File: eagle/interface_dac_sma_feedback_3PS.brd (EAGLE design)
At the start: 95.6 x 144.9 mm, 36 parts, among them IC1 ISO1540, IC2 LT1352PA, IC3 LT1352PA, Q1 TIP122V, Q2 TIP122V, Q3 TIP122V, X1 BU-SMA-V

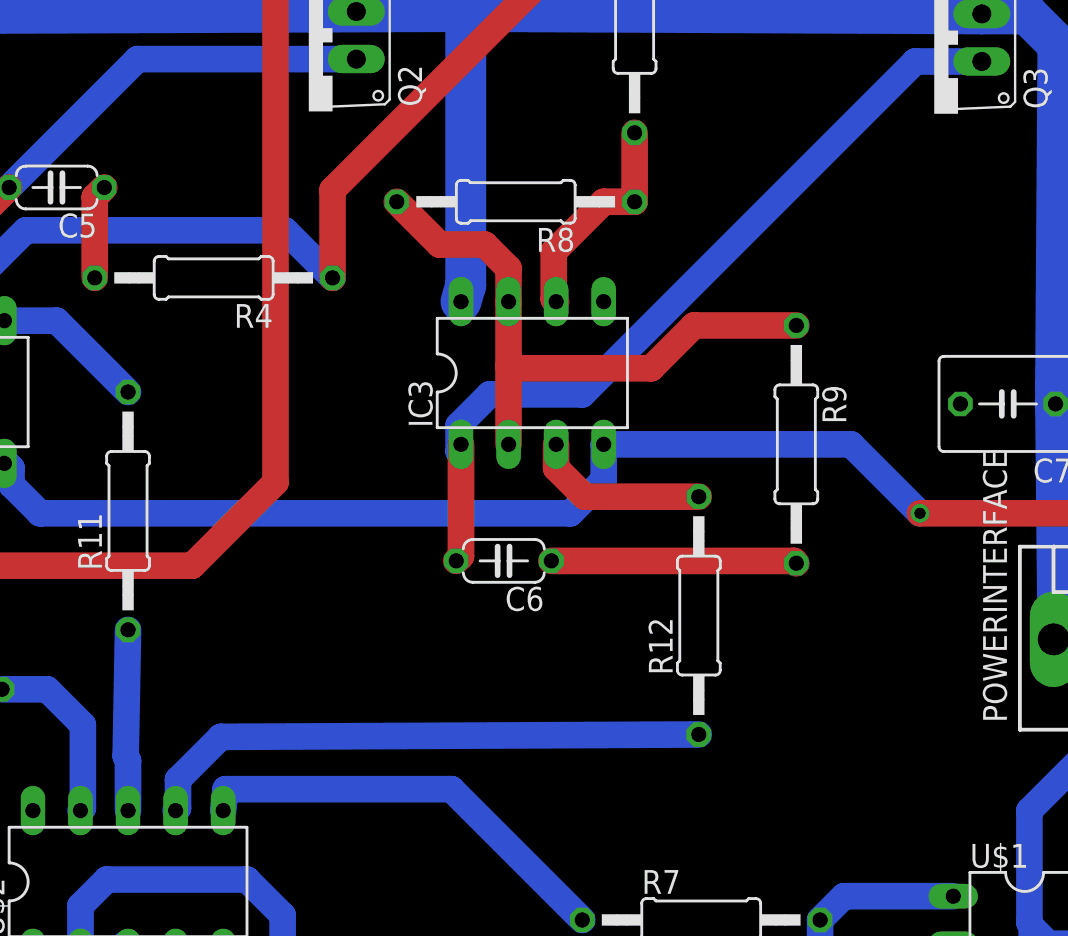
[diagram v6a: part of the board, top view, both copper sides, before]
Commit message: Fix negative rail problems
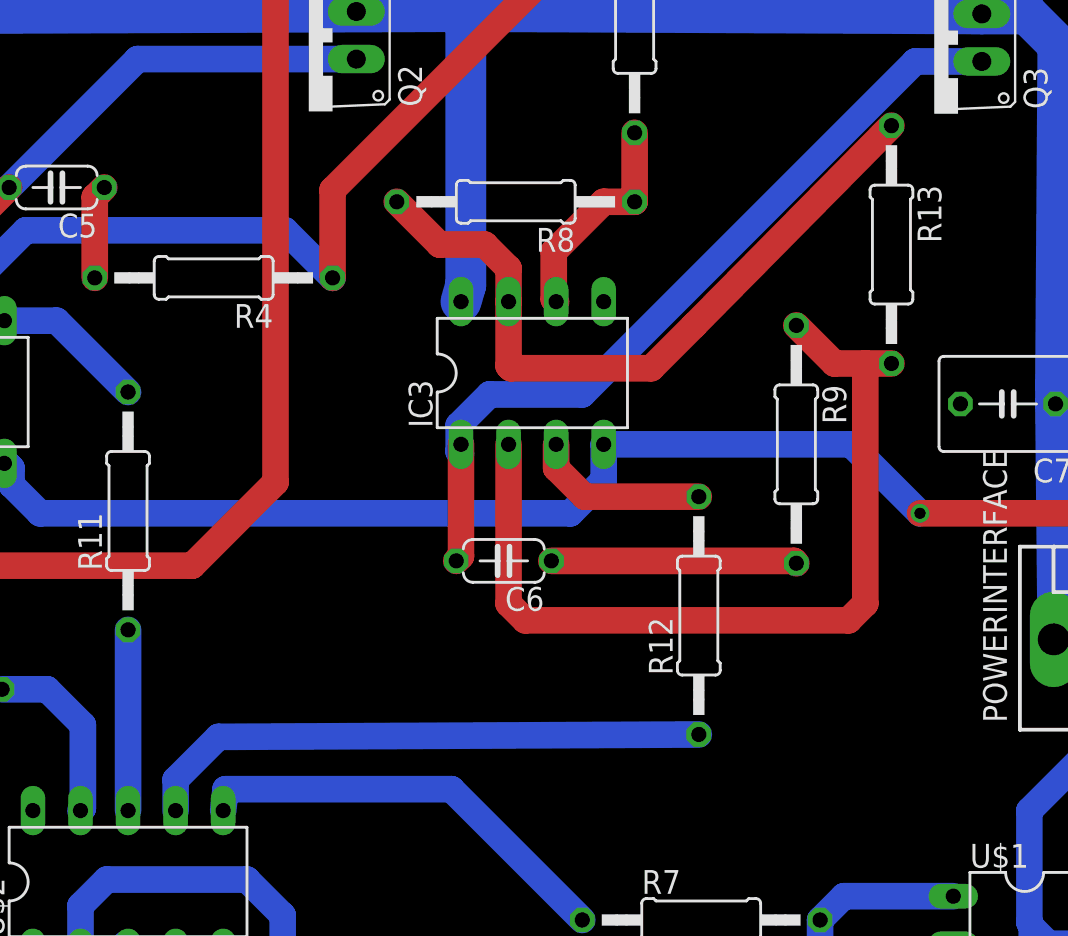
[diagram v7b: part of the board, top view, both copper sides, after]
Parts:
- added R13: 10k, resistor:0207/12
- R12: value 12 -> 10k
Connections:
- new net N$27: IC3.2, R13.2, R9.1
- net N$14: now also R13.1; no longer IC3.2, R9.1
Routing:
- net N$27: track 0.00 -> 47.0 mm
- net N$14: track 33.2 -> 38.6 mm
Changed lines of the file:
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@@
 <element name="R10" library="resistor" package="0207/12" value="10k" x="16.383" y="86.487" rot="R180"/>
 <element name="R11" library="resistor" package="0207/12" value="10k" x="29.464" y="96.012" rot="R90"/>
-<element name="R12" library="resistor" package="0207/12" value="12" x="59.944" y="90.424" rot="R90"/>
+<element name="R12" library="resistor" package="0207/12" value="10k" x="59.944" y="90.424" rot="R90"/>
 <element name="Q1" library="transistor-npn" package="TO220V" value="TIP122V" x="8.763" y="122.555" rot="R90"/>
 <element name="Q2" library="transistor-npn" package="TO220V" value="TIP122V" x="39.116" y="122.682" rot="R90"/>
@@
 <attribute name="OC_FARNELL" value="unknown" x="51.054" y="103.378" size="1.778" layer="27" display="off"/>
 </element>
+<element name="R13" library="resistor" package="0207/12" value="10k" x="70.231" y="110.236" rot="R270"/>
 </elements>
 <signals>
@@
 </signal>
 <signal name="N$14">
-<contactref element="R8" pad="2"/>
-<contactref element="R9" pad="1"/>
-<contactref element="IC3" pad="2"/>
 <contactref element="IC3" pad="7"/>
 <wire x1="49.784" y1="107.188" x2="49.784" y2="108.966" width="1.4224" layer="1"/>
 <wire x1="49.784" y1="108.966" x2="48.514" y2="110.236" width="1.4224" layer="1"/>
 <wire x1="48.514" y1="110.236" x2="46.101" y2="110.236" width="1.4224" layer="1"/>
-<wire x1="46.101" y1="110.236" x2="43.815" y2="112.522" width="1.4224" layer="1"/>
-<wire x1="49.784" y1="99.568" x2="49.784" y2="103.759" width="1.4224" layer="1"/>
 <wire x1="49.784" y1="103.759" x2="49.784" y2="107.188" width="1.4224" layer="1"/>
-<wire x1="65.151" y1="105.918" x2="59.69" y2="105.918" width="1.4224" layer="1"/>
 <wire x1="59.69" y1="105.918" x2="57.404" y2="103.632" width="1.4224" layer="1"/>
 <wire x1="57.404" y1="103.632" x2="49.911" y2="103.632" width="1.4224" layer="1"/>
 <wire x1="49.911" y1="103.632" x2="49.784" y2="103.759" width="1.4224" layer="1"/>
+<contactref element="R8" pad="2"/>
+<contactref element="R13" pad="1"/>
+<wire x1="59.69" y1="105.918" x2="70.231" y2="116.586" width="1.4224" layer="1"/>
+<wire x1="46.101" y1="110.236" x2="43.815" y2="112.522" width="1.4224" layer="1"/>
 </signal>
 <signal name="N$17">
@@
 <contactref element="U$2" pad="7"/>
 <contactref element="R12" pad="1"/>
-<wire x1="59.944" y1="84.074" x2="34.417" y2="83.947" width="1.4224" layer="16"/>
-<wire x1="34.417" y1="83.947" x2="32.131" y2="81.661" width="1.4224" layer="16"/>
-<wire x1="32.131" y1="81.661" x2="32.131" y2="80.137" width="1.4224" layer="16"/>
-<wire x1="32.131" y1="80.137" x2="32.004" y2="80.01" width="1.4224" layer="16"/>
+<wire x1="59.944" y1="84.074" x2="34.29" y2="83.947" width="1.4224" layer="16"/>
+<wire x1="34.29" y1="83.947" x2="32.004" y2="81.661" width="1.4224" layer="16"/>
+<wire x1="32.004" y1="81.661" x2="32.004" y2="80.01" width="1.4224" layer="16"/>
 </signal>
 <signal name="N$26">
 <contactref element="U$2" pad="8"/>
 <contactref element="R11" pad="1"/>
-<wire x1="29.464" y1="89.662" x2="29.337" y2="82.931" width="1.4224" layer="16"/>
-<wire x1="29.337" y1="82.931" x2="29.464" y2="82.677" width="1.4224" layer="16"/>
-<wire x1="29.464" y1="82.677" x2="29.464" y2="80.01" width="1.4224" layer="16"/>
+<wire x1="29.464" y1="89.662" x2="29.464" y2="80.01" width="1.4224" layer="16"/>
 </signal>
 <signal name="N$5">
@@
 <wire x1="41.148" y1="125.73" x2="41.656" y2="125.222" width="2.1844" layer="16"/>
 </signal>
+<signal name="N$27">
+<contactref element="R9" pad="1"/>
+<contactref element="R13" pad="2"/>
+<contactref element="IC3" pad="2"/>
+<wire x1="65.151" y1="105.918" x2="67.183" y2="103.886" width="1.4224" layer="1"/>
+<wire x1="67.183" y1="103.886" x2="68.834" y2="103.886" width="1.4224" layer="1"/>
+<wire x1="68.834" y1="103.886" x2="70.231" y2="103.886" width="1.4224" layer="1"/>
+<wire x1="49.784" y1="99.568" x2="49.784" y2="91.059" width="1.4224" layer="1"/>
+<wire x1="49.784" y1="91.059" x2="50.673" y2="90.17" width="1.4224" layer="1"/>
+<wire x1="50.673" y1="90.17" x2="67.945" y2="90.17" width="1.4224" layer="1"/>
+<wire x1="67.945" y1="90.17" x2="68.834" y2="91.059" width="1.4224" layer="1"/>
+<wire x1="68.834" y1="91.059" x2="68.834" y2="103.886" width="1.4224" layer="1"/>
+</signal>
 </signals>
+<errors>
+</errors>
 </board>
 </drawing>

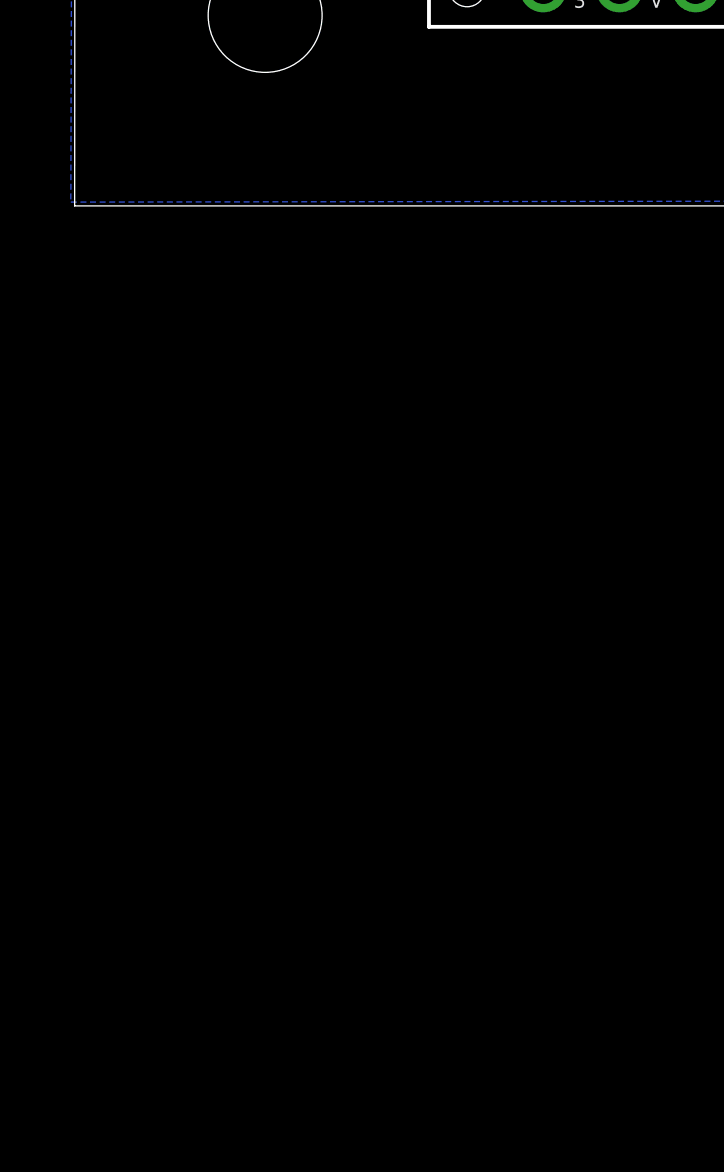
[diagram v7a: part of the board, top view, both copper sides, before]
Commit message: mods to include negative mode, warning before start, voltage readout pins
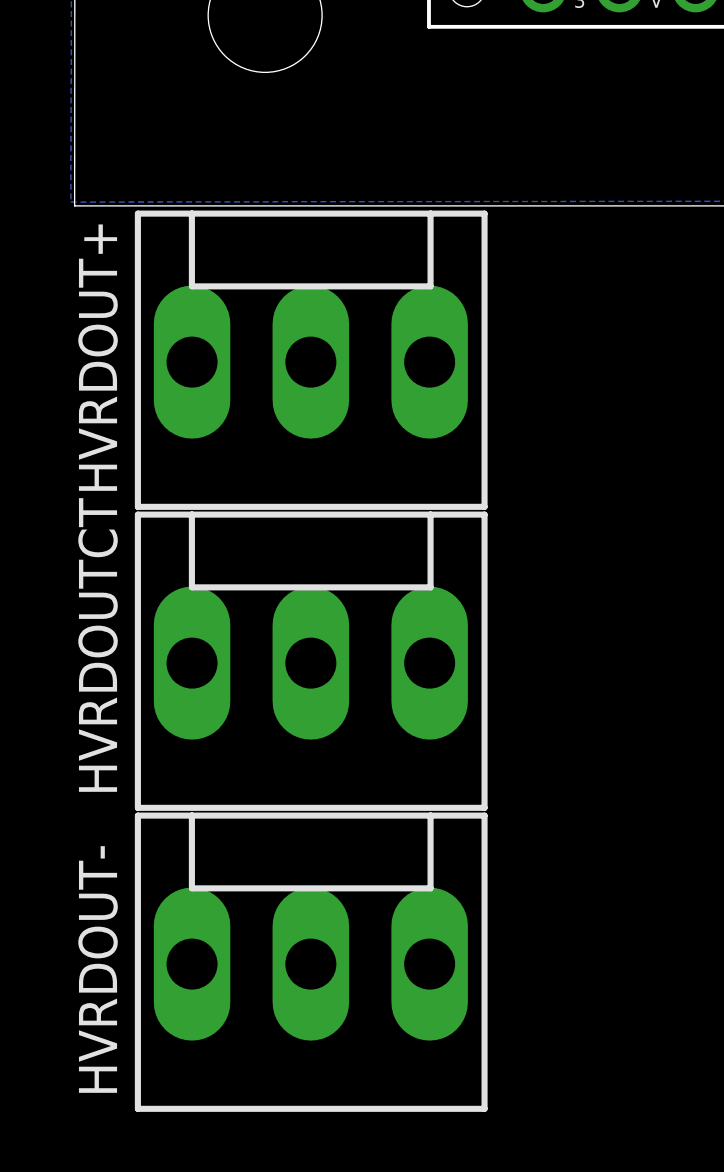
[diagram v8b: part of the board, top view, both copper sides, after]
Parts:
- added HVRDOUT+, HVRDOUT-, HVRDOUTCT: (no value), con-molex:KK-156-3
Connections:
- net +12V: now also HVRDOUT+.1, HVRDOUT-.1, HVRDOUTCT.1
- net GND: now also HVRDOUT+.3, HVRDOUT-.3, HVRDOUTCT.3
- net N$14: now also HVRDOUT-.2
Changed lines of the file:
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@@
 </element>
 <element name="R13" library="resistor" package="0207/12" value="10k" x="70.231" y="110.236" rot="R270"/>
+<element name="HVRDOUT+" library="con-molex" package="KK-156-3" value="" x="7.874" y="-5.207">
+<attribute name="OC_NEWARK" value="unknown" x="7.874" y="-5.207" size="1.778" layer="27" display="off"/>
+<attribute name="MPN" value="" x="7.874" y="-5.207" size="1.778" layer="27" display="off"/>
+<attribute name="MF" value="" x="7.874" y="-5.207" size="1.778" layer="27" display="off"/>
+<attribute name="OC_FARNELL" value="unknown" x="7.874" y="-5.207" size="1.778" layer="27" display="off"/>
+</element>
+<element name="HVRDOUTCT" library="con-molex" package="KK-156-3" value="" x="7.874" y="-15.24">
+<attribute name="OC_NEWARK" value="unknown" x="7.874" y="-15.24" size="1.778" layer="27" display="off"/>
+<attribute name="MPN" value="" x="7.874" y="-15.24" size="1.778" layer="27" display="off"/>
+<attribute name="MF" value="" x="7.874" y="-15.24" size="1.778" layer="27" display="off"/>
+<attribute name="OC_FARNELL" value="unknown" x="7.874" y="-15.24" size="1.778" layer="27" display="off"/>
+</element>
+<element name="HVRDOUT-" library="con-molex" package="KK-156-3" value="" x="7.874" y="-25.273">
+<attribute name="OC_NEWARK" value="unknown" x="7.874" y="-25.273" size="1.778" layer="27" display="off"/>
+<attribute name="MPN" value="" x="7.874" y="-25.273" size="1.778" layer="27" display="off"/>
+<attribute name="MF" value="" x="7.874" y="-25.273" size="1.778" layer="27" display="off"/>
+<attribute name="OC_FARNELL" value="unknown" x="7.874" y="-25.273" size="1.778" layer="27" display="off"/>
+</element>
 </elements>
 <signals>
@@
 <contactref element="C7" pad="2"/>
 <contactref element="IC3" pad="5"/>
+<contactref element="HVRDOUT+" pad="3"/>
+<contactref element="HVRDOUTCT" pad="3"/>
+<contactref element="HVRDOUT-" pad="3"/>
+<wire x1="54.864" y1="107.188" x2="60.423" y2="136.271" width="0" layer="19" extent="1-1"/>
+<wire x1="73.914" y1="101.727" x2="54.864" y2="107.188" width="0" layer="19" extent="1-1"/>
+<wire x1="86.816" y1="89.154" x2="73.914" y2="101.727" width="0" layer="19" extent="1-1"/>
+<wire x1="86.0453" y1="77.9625" x2="86.816" y2="89.154" width="0" layer="19" extent="1-1"/>
+<wire x1="91.1451" y1="77.9625" x2="86.0453" y2="77.9625" width="0" layer="19" extent="1-1"/>
+<wire x1="91.1451" y1="72.8627" x2="91.1451" y2="77.9625" width="0" layer="19" extent="1-1"/>
+<wire x1="86.0453" y1="72.8627" x2="86.0453" y2="77.9625" width="0" layer="19" extent="1-1"/>
+<wire x1="81.153" y1="70.358" x2="86.0453" y2="72.8627" width="0" layer="19" extent="1-1"/>
+<wire x1="73.533" y1="72.898" x2="81.153" y2="70.358" width="0" layer="19" extent="1-1"/>
+<wire x1="61.341" y1="63.881" x2="73.533" y2="72.898" width="0" layer="19" extent="1-1"/>
+<wire x1="60.833" y1="57.531" x2="61.341" y2="63.881" width="0" layer="19" extent="1-1"/>
+<wire x1="68.453" y1="54.991" x2="60.833" y2="57.531" width="0" layer="19" extent="1-1"/>
+<wire x1="53.721" y1="69.215" x2="61.341" y2="63.881" width="0" layer="19" extent="1-1"/>
+<wire x1="52.451" y1="49.149" x2="60.833" y2="57.531" width="0" layer="19" extent="1-1"/>
+<wire x1="86.614" y1="54.483" x2="81.153" y2="70.358" width="0" layer="19" extent="1-1"/>
+<wire x1="32.004" y1="72.39" x2="53.721" y2="69.215" width="0" layer="19" extent="1-1"/>
+<wire x1="24.384" y1="80.01" x2="32.004" y2="72.39" width="0" layer="19" extent="1-1"/>
+<wire x1="10.668" y1="76.402" x2="24.384" y2="80.01" width="0" layer="19" extent="1-1"/>
+<wire x1="19.304" y1="63.246" x2="32.004" y2="72.39" width="0" layer="19" extent="1-1"/>
+<wire x1="15.875" y1="49.022" x2="19.304" y2="63.246" width="0" layer="19" extent="1-1"/>
+<wire x1="30.07" y1="136.017" x2="60.423" y2="136.271" width="0" layer="19" extent="1-1"/>
+<wire x1="11.834" y1="-5.207" x2="15.875" y2="49.022" width="0" layer="19" extent="1-1"/>
+<wire x1="11.834" y1="-15.24" x2="11.834" y2="-5.207" width="0" layer="19" extent="1-1"/>
+<wire x1="11.834" y1="-25.273" x2="11.834" y2="-15.24" width="0" layer="19" extent="1-1"/>
 </signal>
 <signal name="PWM6">
@@
 <wire x1="47.498" y1="122.682" x2="47.498" y2="108.077" width="2.1844" layer="16"/>
 <wire x1="47.498" y1="108.077" x2="47.244" y2="107.188" width="2.1844" layer="16"/>
+<contactref element="HVRDOUT+" pad="1"/>
+<contactref element="HVRDOUTCT" pad="1"/>
+<contactref element="HVRDOUT-" pad="1"/>
 <wire x1="10.541" y1="122.555" x2="11.303" y2="122.555" width="0" layer="19" extent="16-16"/>
+<wire x1="3.914" y1="-5.207" x2="15.24" y2="106.172" width="0" layer="19" extent="1-1"/>
+<wire x1="3.914" y1="-15.24" x2="3.914" y2="-5.207" width="0" layer="19" extent="1-1"/>
+<wire x1="3.914" y1="-25.273" x2="3.914" y2="-15.24" width="0" layer="19" extent="1-1"/>
 </signal>
 <signal name="N$2">
@@
 <wire x1="59.69" y1="105.918" x2="70.231" y2="116.586" width="1.4224" layer="1"/>
 <wire x1="46.101" y1="110.236" x2="43.815" y2="112.522" width="1.4224" layer="1"/>
+<contactref element="HVRDOUT-" pad="2"/>
+<wire x1="7.874" y1="-25.273" x2="49.911" y2="103.632" width="0" layer="19" extent="1-1"/>
 </signal>
 <signal name="N$17">
